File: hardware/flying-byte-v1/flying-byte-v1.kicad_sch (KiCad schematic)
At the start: 24 parts, among them J1 Conn_Coaxial, U1 STM32WB55CEU6, X1 32MHz, X2 32kHz768

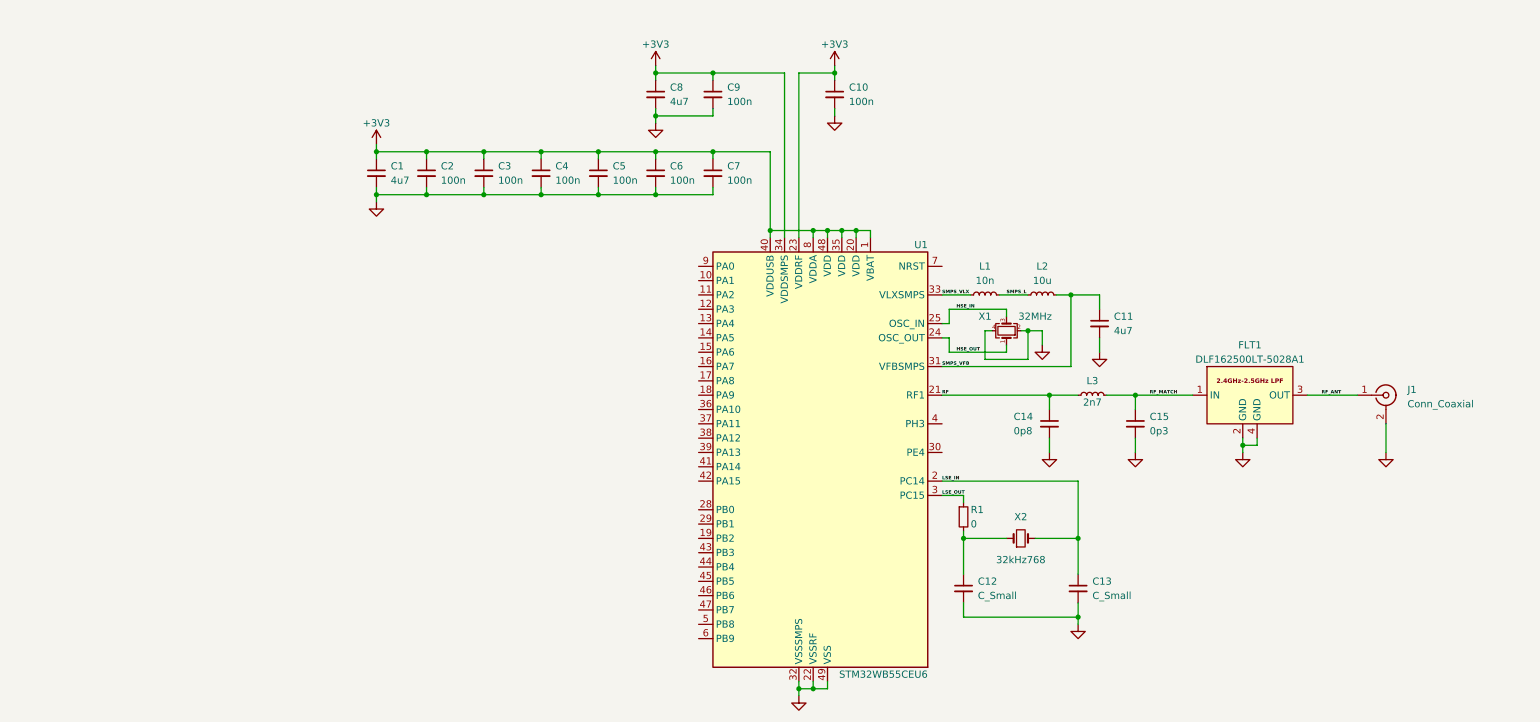
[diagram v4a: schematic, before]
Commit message: feature: Add the SWD programming interface
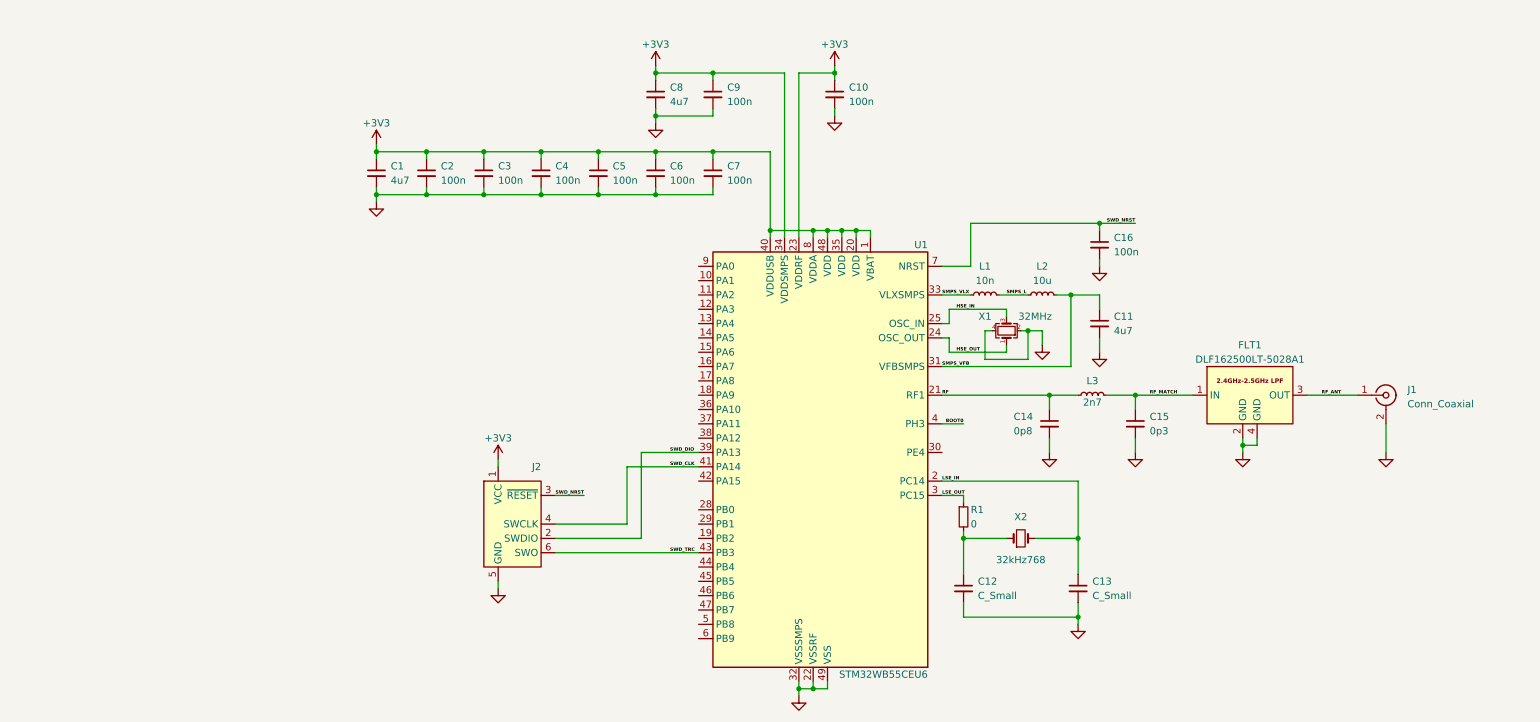
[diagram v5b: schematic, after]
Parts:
- added C16: 100n, symbol Device:C_Small
- added J2: Conn_ARM_SWD_TagConnect_TC2030, Connector:Tag-Connect_TC2030-IDC-FP_2x03_P1.27mm_Vertical, symbol Connector:Conn_ARM_SWD_TagConnect_TC2030
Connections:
- net +3V3: now also J2.1 (VCC)
- net GND: now also C16.2, J2.5 (GND)
- net SWD_DIO: now reaches U1.39 (PA13)
- net SWD_DIO: now also J2.2 (SWDIO)
- net BOOT0: now reaches U1.4 (PH3)
- net SWD_CLK: now reaches U1.41 (PA14)
- net SWD_CLK: now also J2.4 (SWCLK)
- net SWD_TRC: now reaches U1.43 (PB3)
- net SWD_TRC: now also J2.6 (SWO)
- net SWD_NRST: now reaches U1.7 (NRST)
- net SWD_NRST: now also C16.1, J2.3 (~{RESET})
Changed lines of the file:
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@@
   (junction (at 130.81 50.8) (diameter 0) (color 0 0 0 0)
   )
+  (junction (at 209.55 55.88) (diameter 0) (color 0 0 0 0)
+  )
   (junction (at 130.81 36.83) (diameter 0) (color 0 0 0 0)
   )
@@
     (stroke (width 0) (type default))
   )
+  (wire (pts (xy 113.03 114.3) (xy 138.43 114.3))
+    (stroke (width 0) (type default))
+  )
+  (wire (pts (xy 186.69 55.88) (xy 209.55 55.88))
+    (stroke (width 0) (type default))
+  )
   (wire (pts (xy 162.56 35.56) (xy 162.56 36.83))
     (stroke (width 0) (type default))
@@
     (stroke (width 0) (type default))
   )
+  (wire (pts (xy 209.55 55.88) (xy 209.55 57.15))
+    (stroke (width 0) (type default))
+  )
   (wire (pts (xy 161.29 58.42) (xy 161.29 57.15))
     (stroke (width 0) (type default))
@@
     (stroke (width 0) (type default))
   )
+  (wire (pts (xy 209.55 55.88) (xy 215.9 55.88))
+    (stroke (width 0) (type default))
+  )
   (wire (pts (xy 156.21 138.43) (xy 156.21 139.7))
     (stroke (width 0) (type default))
@@
     (stroke (width 0) (type default))
   )
+  (wire (pts (xy 181.61 91.44) (xy 185.42 91.44))
+    (stroke (width 0) (type default))
+  )
   (wire (pts (xy 193.04 78.74) (xy 193.04 77.47))
     (stroke (width 0) (type default))
@@
     (stroke (width 0) (type default))
   )
+  (wire (pts (xy 102.87 119.38) (xy 102.87 120.65))
+    (stroke (width 0) (type default))
+  )
+  (wire (pts (xy 113.03 104.14) (xy 118.11 104.14))
+    (stroke (width 0) (type default))
+  )
   (wire (pts (xy 195.58 74.93) (xy 196.85 74.93))
     (stroke (width 0) (type default))
   )
+  (wire (pts (xy 125.73 99.06) (xy 138.43 99.06))
+    (stroke (width 0) (type default))
+  )
   (wire (pts (xy 100.33 43.18) (xy 100.33 44.45))
     (stroke (width 0) (type default))
@@
     (stroke (width 0) (type default))
   )
+  (wire (pts (xy 128.27 96.52) (xy 128.27 111.76))
+    (stroke (width 0) (type default))
+  )
   (wire (pts (xy 90.17 50.8) (xy 81.28 50.8))
     (stroke (width 0) (type default))
   )
+  (wire (pts (xy 125.73 99.06) (xy 125.73 109.22))
+    (stroke (width 0) (type default))
+  )
   (wire (pts (xy 246.38 86.36) (xy 255.27 86.36))
     (stroke (width 0) (type default))
@@
     (stroke (width 0) (type default))
   )
+  (wire (pts (xy 209.55 62.23) (xy 209.55 63.5))
+    (stroke (width 0) (type default))
+  )
   (wire (pts (xy 81.28 41.91) (xy 81.28 43.18))
     (stroke (width 0) (type default))
@@
     (stroke (width 0) (type default))
   )
+  (wire (pts (xy 181.61 63.5) (xy 186.69 63.5))
+    (stroke (width 0) (type default))
+  )
   (wire (pts (xy 110.49 50.8) (xy 100.33 50.8))
     (stroke (width 0) (type default))
@@
     (stroke (width 0) (type default))
   )
+  (wire (pts (xy 102.87 97.79) (xy 102.87 99.06))
+    (stroke (width 0) (type default))
+  )
+  (wire (pts (xy 186.69 63.5) (xy 186.69 55.88))
+    (stroke (width 0) (type default))
+  )
   (wire (pts (xy 189.23 74.93) (xy 189.23 80.01))
     (stroke (width 0) (type default))
@@
     (stroke (width 0) (type default))
   )
+  (wire (pts (xy 128.27 111.76) (xy 113.03 111.76))
+    (stroke (width 0) (type default))
+  )
   (wire (pts (xy 181.61 86.36) (xy 200.66 86.36))
     (stroke (width 0) (type default))
@@
     (stroke (width 0) (type default))
   )
+  (wire (pts (xy 113.03 109.22) (xy 125.73 109.22))
+    (stroke (width 0) (type default))
+  )
   (wire (pts (xy 204.47 68.58) (xy 209.55 68.58))
     (stroke (width 0) (type default))
@@
   (wire (pts (xy 130.81 30.48) (xy 130.81 29.21))
     (stroke (width 0) (type default))
+  )
+  (wire (pts (xy 128.27 96.52) (xy 138.43 96.52))
+    (stroke (width 0) (type default))
+  )
+  (label "SWD_DIO" (at 133.35 96.52 0) (fields_autoplaced)
+    (effects (font (size 0.6 0.6) (thickness 0.21) bold) (justify left bottom))
+  )
+  (label "SWD_TRC" (at 133.35 114.3 0) (fields_autoplaced)
+    (effects (font (size 0.6 0.6) (thickness 0.21) bold) (justify left bottom))
   )
   (label "RF_MATCH" (at 218.44 86.36 0) (fields_autoplaced)
@@
     (effects (font (size 0.6 0.6) (thickness 0.21) bold) (justify left bottom))
   )
+  (label "BOOT0" (at 185.42 91.44 180) (fields_autoplaced)
+    (effects (font (size 0.6 0.6) (thickness 0.21) bold) (justify right bottom))
+  )
   (label "SMPS_VLX" (at 181.61 68.58 0) (fields_autoplaced)
     (effects (font (size 0.6 0.6) (thickness 0.21) bold) (justify left bottom))
@@
     (effects (font (size 0.6 0.6) (thickness 0.21) bold) (justify left bottom))
   )
+  (label "SWD_CLK" (at 133.35 99.06 0) (fields_autoplaced)
+    (effects (font (size 0.6 0.6) (thickness 0.21) bold) (justify left bottom))
+  )
   (label "HSE_OUT" (at 184.15 78.74 0) (fields_autoplaced)
     (effects (font (size 0.6 0.6) (thickness 0.21) bold) (justify left bottom))
@@
   (label "RF_ANT" (at 248.92 86.36 0) (fields_autoplaced)
     (effects (font (size 0.6 0.6) (thickness 0.21) bold) (justify left bottom))
+  )
+  (label "SWD_NRST" (at 118.11 104.14 180) (fields_autoplaced)
+    (effects (font (size 0.6 0.6) (thickness 0.21) bold) (justify right bottom))
+  )
+  (label "SWD_NRST" (at 215.9 55.88 180) (fields_autoplaced)
+    (effects (font (size 0.6 0.6) (thickness 0.21) bold) (justify right bottom))
   )
   (symbol (lib_id "Device:L_Small") (at 199.39 68.58 90) (unit 1)
@@
     )
   )
+  (symbol (lib_id "Connector:Conn_ARM_SWD_TagConnect_TC2030") (at 105.41 109.22 0) (unit 1)
+    (in_bom no) (on_board yes) (dnp no)
+    (property "Reference" "J2" (at 110.49 99.06 0)
+      (effects (font (size 1.27 1.27)) (justify right))
+    )
+    (property "Value" "Conn_ARM_SWD_TagConnect_TC2030" (at 99.06 110.49 0)
+      (effects (font (size 1.27 1.27)) (justify right) hide)
+    )
+    (property "Footprint" "Connector:Tag-Connect_TC2030-IDC-FP_2x03_P1.27mm_Vertical" (at 105.41 127 0)
+      (effects (font (size 1.27 1.27)) hide)
+    )
+    (property "Datasheet" "https://www.tag-connect.com/wp-content/uploads/bsk-pdf-manager/TC2030-CTX_1.pdf" (at 105.41 124.46 0)
+      (effects (font (size 1.27 1.27)) hide)
+    )
+    (pin "1")
+    (pin "2")
+    (pin "3")
+    (pin "4")
+    (pin "5")
+    (pin "6")
+    (instances
+      (project "flying-byte-v1"
+        (path "/89251f6d-2a03-4ee6-93f4-15acd18dfc68"
+          (reference "J2") (unit 1)
+        )
+      )
+    )
+  )
   (symbol (lib_id "Device:Crystal_GND24_Small") (at 193.04 74.93 90) (unit 1)
     (in_bom yes) (on_board yes) (dnp no)
@@
     )
   )
+  (symbol (lib_id "power:+3V3") (at 102.87 97.79 0) (unit 1)
+    (in_bom yes) (on_board yes) (dnp no)
+    (property "Reference" "#PWR016" (at 102.87 101.6 0)
+      (effects (font (size 1.27 1.27)) hide)
+    )
+    (property "Value" "+3V3" (at 102.87 93.98 0)
+      (effects (font (size 1.27 1.27)))
+    )
+    (property "Footprint" "" (at 102.87 97.79 0)
+      (effects (font (size 1.27 1.27)) hide)
+    )
+    (property "Datasheet" "" (at 102.87 97.79 0)
+      (effects (font (size 1.27 1.27)) hide)
+    )
+    (pin "1")
+    (instances
+      (project "flying-byte-v1"
+        (path "/89251f6d-2a03-4ee6-93f4-15acd18dfc68"
+          (reference "#PWR016") (unit 1)
+        )
+      )
+    )
+  )
   (symbol (lib_id "Device:C_Small") (at 90.17 46.99 0) (unit 1)
     (in_bom yes) (on_board yes) (dnp no) (fields_autoplaced)
@@
         (path "/89251f6d-2a03-4ee6-93f4-15acd18dfc68"
           (reference "C2") (unit 1)
+        )
+      )
+    )
+  )
+  (symbol (lib_id "power:GND") (at 209.55 63.5 0) (unit 1)
+    (in_bom yes) (on_board yes) (dnp no) (fields_autoplaced)
+    (property "Reference" "#PWR017" (at 209.55 69.85 0)
+      (effects (font (size 1.27 1.27)) hide)
+    )
+    (property "Value" "GND" (at 209.55 68.58 0)
+      (effects (font (size 1.27 1.27)) hide)
+    )
+    (property "Footprint" "" (at 209.55 63.5 0)
+      (effects (font (size 1.27 1.27)) hide)
+    )
+    (property "Datasheet" "" (at 209.55 63.5 0)
+      (effects (font (size 1.27 1.27)) hide)
+    )
+    (pin "1")
+    (instances
+      (project "flying-byte-v1"
+        (path "/89251f6d-2a03-4ee6-93f4-15acd18dfc68"
+          (reference "#PWR017") (unit 1)
         )
       )
@@
     )
   )
+  (symbol (lib_id "Device:C_Small") (at 209.55 59.69 0) (unit 1)
+    (in_bom yes) (on_board yes) (dnp no) (fields_autoplaced)
+    (property "Reference" "C16" (at 212.09 58.4263 0)
+      (effects (font (size 1.27 1.27)) (justify left))
+    )
+    (property "Value" "100n" (at 212.09 60.9663 0)
+      (effects (font (size 1.27 1.27)) (justify left))
+    )
+    (property "Footprint" "" (at 209.55 59.69 0)
+      (effects (font (size 1.27 1.27)) hide)
+    )
+    (property "Datasheet" "~" (at 209.55 59.69 0)
+      (effects (font (size 1.27 1.27)) hide)
+    )
+    (pin "1")
+    (pin "2")
+    (instances
+      (project "flying-byte-v1"
+        (path "/89251f6d-2a03-4ee6-93f4-15acd18dfc68"
+          (reference "C16") (unit 1)
+        )
+      )
+    )
+  )
   (symbol (lib_id "Device:C_Small") (at 185.42 120.65 0) (unit 1)
     (in_bom yes) (on_board yes) (dnp no) (fields_autoplaced)
@@
         )
       )
+    )
+  )
+  (symbol (lib_id "power:GND") (at 102.87 120.65 0) (unit 1)
+    (in_bom yes) (on_board yes) (dnp no) (fields_autoplaced)
+    (property "Reference" "#PWR015" (at 102.87 127 0)
+      (effects (font (size 1.27 1.27)) hide)
+    )
+    (property "Value" "GND" (at 102.87 125.73 0)
+      (effects (font (size 1.27 1.27)) hide)
+    )
+    (property "Footprint" "" (at 102.87 120.65 0)
+      (effects (font (size 1.27 1.27)) hide)
+    )
+    (property "Datasheet" "" (at 102.87 120.65 0)
+      (effects (font (size 1.27 1.27)) hide)
+    )
+    (pin "1")
+    (instances
+      (project "flying-byte-v1"
+        (path "/89251f6d-2a03-4ee6-93f4-15acd18dfc68"
+          (reference "#PWR015") (unit 1)
+        )
+      )
